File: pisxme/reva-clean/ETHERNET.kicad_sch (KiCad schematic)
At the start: 0 parts

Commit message: add native Phase 3 contract connectivity
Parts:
- added X: ETHERNET_Contract
- added XET: ETHERNET_Contract, symbol PiSXMeRevAClean:ETHERNET_Contract
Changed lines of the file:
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@@
 (kicad_sch (version 20230409) (generator "eeschema")
   (paper "A4")
+    (symbol "PiSXMeRevAClean:ETHERNET_Contract"
+      (pin_names (offset 1.0))
+      (exclude_from_sim no)
+      (in_bom yes)
+      (on_board yes)
+      (property "Reference" "X"
+        (at 0 -7.039999999999999 0)
+        (effects (font (size 1.27 1.27))))
+      (property "Value" "ETHERNET_Contract"
+        (at 0 7.039999999999999 0)
+        (effects (font (size 1.27 1.27))))
+      (property "Footprint" ""
+        (at 0 0 0)
+        (effects (font (size 1.27 1.27)) (hide yes)))
+      (property "Datasheet" "~"
+        (at 0 0 0)
+        (effects (font (size 1.27 1.27)) (hide yes)))
+      (symbol "ETHERNET_Contract_1_1"
+        (rectangle (start -1.27 -5.77) (end 1.27 5.77)
+          (stroke (width 0.254) (type default)) (fill (type background)))
+        (pin passive line
+          (at -5.08 0 0)
+          (length 3.81)
+          (name "CM5_GBE" (effects (font (size 1.27 1.27))))
+          (number "1" (effects (font (size 1.27 1.27)))))
+        (pin passive line
+          (at -5.08 3 0)
+          (length 3.81)
+          (name "GBE_LED" (effects (font (size 1.27 1.27))))
+          (number "2" (effects (font (size 1.27 1.27)))))
+        (pin passive line
+          (at -5.08 6 0)
+          (length 3.81)
+          (name "GBE_SHIELD" (effects (font (size 1.27 1.27))))
+          (number "3" (effects (font (size 1.27 1.27)))))
+        (pin passive line
+          (at -5.08 9 0)
+          (length 3.81)
+          (name "ETH_POWER" (effects (font (size 1.27 1.27))))
+          (number "4" (effects (font (size 1.27 1.27)))))
+      )
+    )
   (hierarchical_label "CM5_GBE"
     (shape bidirectional)
@@
     (effects (font (size 1.27 1.27)) (justify left))
 )
-  (sheet_instances (path "/6" (page "6")))
+  (wire
+    (pts (xy 5 10) (xy 19.92 10))
+    (stroke (width 0) (type default))
 )
+  (wire
+    (pts (xy 5 13) (xy 19.92 13))
+    (stroke (width 0) (type default))
+)
+  (wire
+    (pts (xy 5 16) (xy 19.92 16))
+    (stroke (width 0) (type default))
+)
+  (wire
+    (pts (xy 5 19) (xy 19.92 19))
+    (stroke (width 0) (type default))
+)
+  (symbol
+    (lib_id "PiSXMeRevAClean:ETHERNET_Contract")
+    (at 25 10 0)
+    (unit 1)
+    (exclude_from_sim no)
+    (in_bom no)
+    (on_board no)
+    (dnp no)
+    (property "Reference" "XET"
+      (at 25 5 0)
+      (effects (font (size 1.27 1.27))))
+    (property "Value" "ETHERNET_Contract"
+      (at 25 18 0)
+      (effects (font (size 1.27 1.27))))
+    (property "Footprint" ""
+      (at 25 10 0)
+      (effects (font (size 1.27 1.27)) (hide yes)))
+    (property "Datasheet" "~"
+      (at 25 10 0)
+      (effects (font (size 1.27 1.27)) (hide yes)))
+    (pin "1")
+    (pin "2")
+    (pin "3")
+    (pin "4")
+    (instances (project "PiSXMe_RevA_Clean"
+      (path "/30000000-0000-0000-0000-000000000000/10000000-0000-0000-0000-000000000006" (reference "XET" ) (unit 1))))
+  )
+  (sheet_instances (path "/30000000-0000-0000-0000-000000000000/10000000-0000-0000-0000-000000000006" (page "6")))
+)

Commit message: close native Phase 3 hierarchy association
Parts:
- removed X: ETHERNET_Contract
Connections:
- net CM5_GBE: now also XET.1 (CM5_GBE)
- net ETH_POWER: now also XET.4 (ETH_POWER)
- net GBE_LED: now also XET.2 (GBE_LED)
- net GBE_SHIELD: now also XET.3 (GBE_SHIELD)
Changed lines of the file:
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@@
 (kicad_sch (version 20230409) (generator "eeschema")
   (paper "A4")
-    (symbol "PiSXMeRevAClean:ETHERNET_Contract"
-      (pin_names (offset 1.0))
-      (exclude_from_sim no)
-      (in_bom yes)
-      (on_board yes)
-      (property "Reference" "X"
-        (at 0 -7.039999999999999 0)
-        (effects (font (size 1.27 1.27))))
-      (property "Value" "ETHERNET_Contract"
-        (at 0 7.039999999999999 0)
-        (effects (font (size 1.27 1.27))))
-      (property "Footprint" ""
-        (at 0 0 0)
-        (effects (font (size 1.27 1.27)) (hide yes)))
-      (property "Datasheet" "~"
-        (at 0 0 0)
-        (effects (font (size 1.27 1.27)) (hide yes)))
-      (symbol "ETHERNET_Contract_1_1"
-        (rectangle (start -1.27 -5.77) (end 1.27 5.77)
-          (stroke (width 0.254) (type default)) (fill (type background)))
-        (pin passive line
-          (at -5.08 0 0)
-          (length 3.81)
-          (name "CM5_GBE" (effects (font (size 1.27 1.27))))
-          (number "1" (effects (font (size 1.27 1.27)))))
-        (pin passive line
-          (at -5.08 3 0)
-          (length 3.81)
-          (name "GBE_LED" (effects (font (size 1.27 1.27))))
-          (number "2" (effects (font (size 1.27 1.27)))))
-        (pin passive line
-          (at -5.08 6 0)
-          (length 3.81)
-          (name "GBE_SHIELD" (effects (font (size 1.27 1.27))))
-          (number "3" (effects (font (size 1.27 1.27)))))
-        (pin passive line
-          (at -5.08 9 0)
-          (length 3.81)
-          (name "ETH_POWER" (effects (font (size 1.27 1.27))))
-          (number "4" (effects (font (size 1.27 1.27)))))
-      )
-    )
   (hierarchical_label "CM5_GBE"
     (shape bidirectional)
-    (at 5 10 0)
-    (effects (font (size 1.27 1.27)) (justify left))
+    (at 5 10 180)
+    (effects (font (size 1.27 1.27)) (justify right))
 )
   (hierarchical_label "GBE_LED"
     (shape bidirectional)
-    (at 5 13 0)
-    (effects (font (size 1.27 1.27)) (justify left))
+    (at 5 13 180)
+    (effects (font (size 1.27 1.27)) (justify right))
 )
   (hierarchical_label "GBE_SHIELD"
     (shape bidirectional)
-    (at 5 16 0)
-    (effects (font (size 1.27 1.27)) (justify left))
+    (at 5 16 180)
+    (effects (font (size 1.27 1.27)) (justify right))
 )
   (hierarchical_label "ETH_POWER"
     (shape bidirectional)
-    (at 5 19 0)
-    (effects (font (size 1.27 1.27)) (justify left))
+    (at 5 19 180)
+    (effects (font (size 1.27 1.27)) (justify right))
 )
   (wire

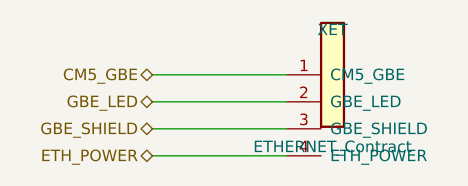
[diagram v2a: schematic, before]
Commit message: stabilize Phase 3 hierarchy netlist references
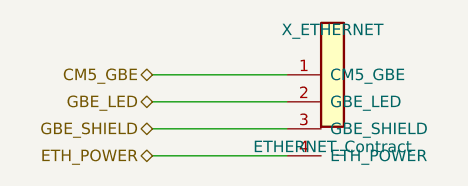
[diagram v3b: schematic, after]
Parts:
- renumbered XET to X_ETHERNET
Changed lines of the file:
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@@
     (on_board no)
     (dnp no)
-    (property "Reference" "XET"
+    (property "Reference" "X_ETHERNET"
       (at 25 5 0)
       (effects (font (size 1.27 1.27))))
@@
     (pin "4")
     (instances (project "PiSXMe_RevA_Clean"
-      (path "/30000000-0000-0000-0000-000000000000/10000000-0000-0000-0000-000000000006" (reference "XET" ) (unit 1))))
+      (path "/30000000-0000-0000-0000-000000000000/10000000-0000-0000-0000-000000000006" (reference "X_ETHERNET" ) (unit 1))))
   )
   (sheet_instances (path "/30000000-0000-0000-0000-000000000000/10000000-0000-0000-0000-000000000006" (page "6")))

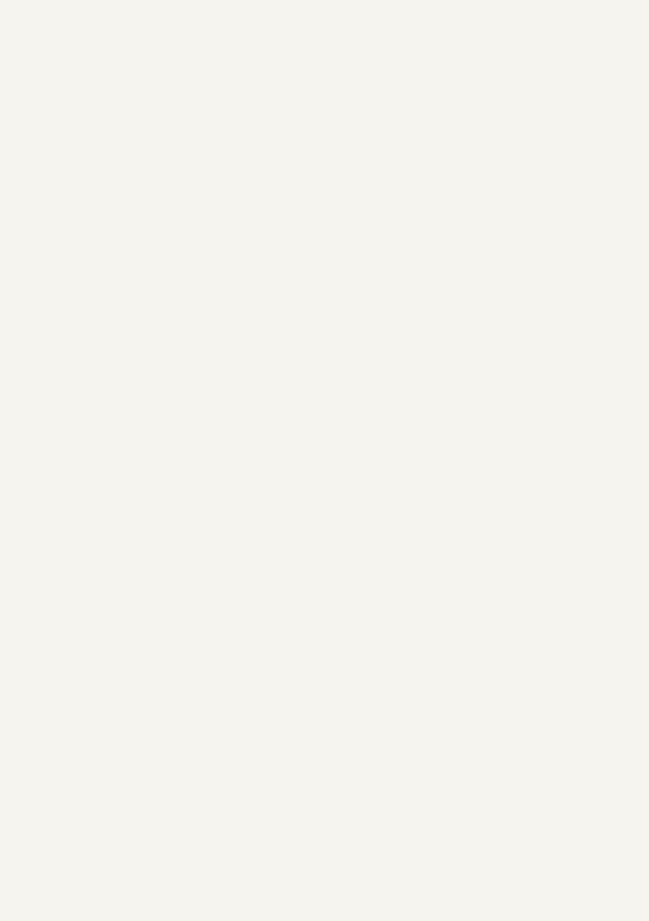
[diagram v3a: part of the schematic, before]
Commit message: close Phase 6 Ethernet island
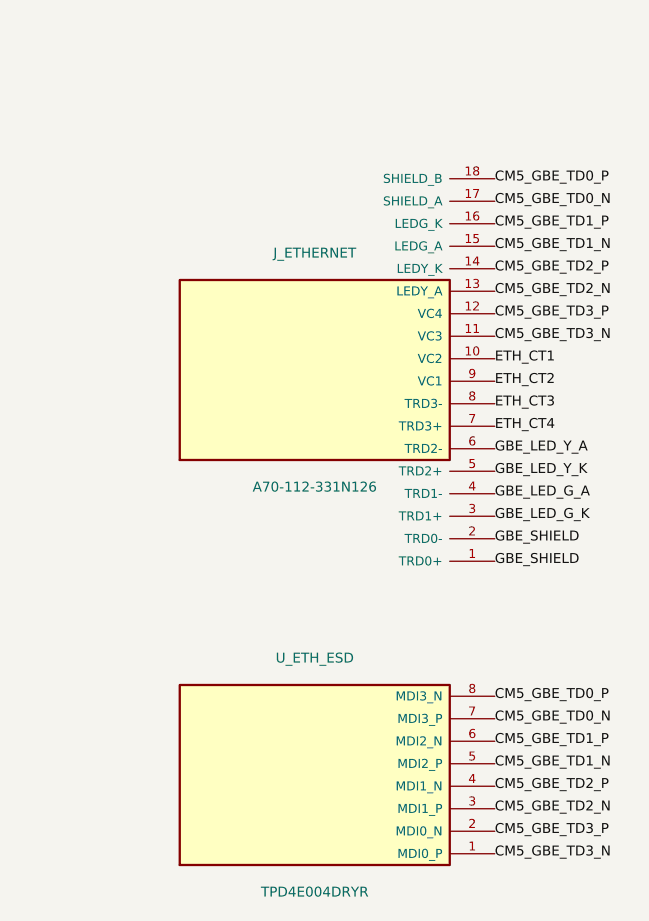
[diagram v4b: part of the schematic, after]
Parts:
- added J_ETHERNET: A70-112-331N126, PiSXMeRevAClean:EDAC_A70_112_331N126, symbol PiSXMeRevAClean:EDAC_A70_112_331N126_Ethernet
- added U_ETH_ESD: TPD4E004DRYR, Package_DFN_QFN:WSON-6-1EP_1.5x1.5mm_P0.5mm_EP0.95x0.95mm, symbol PiSXMeRevAClean:TPD4E004DRYR
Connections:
- net GBE_SHIELD: now also J_ETHERNET.1 (TRD0+), J_ETHERNET.2 (TRD0-)
- new net CM5_GBE_TD0_N: J_ETHERNET.17 (SHIELD_A), U_ETH_ESD.7 (MDI3_P)
- new net CM5_GBE_TD0_P: J_ETHERNET.18 (SHIELD_B), U_ETH_ESD.8 (MDI3_N)
- new net CM5_GBE_TD1_N: J_ETHERNET.15 (LEDG_A), U_ETH_ESD.5 (MDI2_P)
- new net CM5_GBE_TD1_P: J_ETHERNET.16 (LEDG_K), U_ETH_ESD.6 (MDI2_N)
- new net CM5_GBE_TD2_N: J_ETHERNET.13 (LEDY_A), U_ETH_ESD.3 (MDI1_P)
- new net CM5_GBE_TD2_P: J_ETHERNET.14 (LEDY_K), U_ETH_ESD.4 (MDI1_N)
- new net CM5_GBE_TD3_N: J_ETHERNET.11 (VC3), U_ETH_ESD.1 (MDI0_P)
- new net CM5_GBE_TD3_P: J_ETHERNET.12 (VC4), U_ETH_ESD.2 (MDI0_N)
- new net ETH_CT1: J_ETHERNET.10 (VC2)
- new net ETH_CT2: J_ETHERNET.9 (VC1)
- new net ETH_CT3: J_ETHERNET.8 (TRD3-)
- new net ETH_CT4: J_ETHERNET.7 (TRD3+)
- new net GBE_LED_G_A: J_ETHERNET.4 (TRD1-)
- new net GBE_LED_G_K: J_ETHERNET.3 (TRD1+)
- new net GBE_LED_Y_A: J_ETHERNET.6 (TRD2-)
- new net GBE_LED_Y_K: J_ETHERNET.5 (TRD2+)
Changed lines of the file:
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@@
       (path "/30000000-0000-0000-0000-000000000000/10000000-0000-0000-0000-000000000006" (reference "X_ETHERNET" ) (unit 1))))
   )
+(label "CM5_GBE_TD0_P" (at 70 78.75 0) (effects (font (size 1.1 1.1)) (justify left)))
+(label "CM5_GBE_TD0_N" (at 70 81.25 0) (effects (font (size 1.1 1.1)) (justify left)))
+(label "CM5_GBE_TD1_P" (at 70 83.75 0) (effects (font (size 1.1 1.1)) (justify left)))
+(label "CM5_GBE_TD1_N" (at 70 86.25 0) (effects (font (size 1.1 1.1)) (justify left)))
+(label "CM5_GBE_TD2_P" (at 70 88.75 0) (effects (font (size 1.1 1.1)) (justify left)))
+(label "CM5_GBE_TD2_N" (at 70 91.25 0) (effects (font (size 1.1 1.1)) (justify left)))
+(label "CM5_GBE_TD3_P" (at 70 93.75 0) (effects (font (size 1.1 1.1)) (justify left)))
+(label "CM5_GBE_TD3_N" (at 70 96.25 0) (effects (font (size 1.1 1.1)) (justify left)))
+(label "ETH_CT1" (at 70 98.75 0) (effects (font (size 1.1 1.1)) (justify left)))
+(label "ETH_CT2" (at 70 101.25 0) (effects (font (size 1.1 1.1)) (justify left)))
+(label "ETH_CT3" (at 70 103.75 0) (effects (font (size 1.1 1.1)) (justify left)))
+(label "ETH_CT4" (at 70 106.25 0) (effects (font (size 1.1 1.1)) (justify left)))
+(label "GBE_LED_Y_A" (at 70 108.75 0) (effects (font (size 1.1 1.1)) (justify left)))
+(label "GBE_LED_Y_K" (at 70 111.25 0) (effects (font (size 1.1 1.1)) (justify left)))
+(label "GBE_LED_G_A" (at 70 113.75 0) (effects (font (size 1.1 1.1)) (justify left)))
+(label "GBE_LED_G_K" (at 70 116.25 0) (effects (font (size 1.1 1.1)) (justify left)))
+(label "GBE_SHIELD" (at 70 118.75 0) (effects (font (size 1.1 1.1)) (justify left)))
+(label "GBE_SHIELD" (at 70 121.25 0) (effects (font (size 1.1 1.1)) (justify left)))
+(symbol (lib_id "PiSXMeRevAClean:EDAC_A70_112_331N126_Ethernet") (at 50 100 0) (unit 1) (exclude_from_sim no) (in_bom yes) (on_board yes) (dnp no) (property "Reference" "J_ETHERNET" (at 50 87 0) (effects (font (size 1.1 1.1)))) (property "Value" "A70-112-331N126" (at 50 113 0) (effects (font (size 1.1 1.1)))) (property "MPN" "A70-112-331N126" (at 50 100 0) (effects (font (size 1 1)) (hide yes))) (property "Footprint" "PiSXMeRevAClean:EDAC_A70_112_331N126" (at 50 100 0) (effects (font (size 1 1)) (hide yes))) (pin "1")
+(pin "2")
+(pin "3")
+(pin "4")
+(pin "5")
+(pin "6")
+(pin "7")
+(pin "8")
+(pin "9")
+(pin "10")
+(pin "11")
+(pin "12")
+(pin "13")
+(pin "14")
+(pin "15")
+(pin "16")
+(pin "17")
+(pin "18") (instances (project "PiSXMe_RevA_Clean" (path "/30000000-0000-0000-0000-000000000000" (reference "J_ETHERNET") (unit 1)))) )(label "CM5_GBE_TD0_P" (at 70 136.25 0) (effects (font (size 1.1 1.1)) (justify left)))
+(label "CM5_GBE_TD0_N" (at 70 138.75 0) (effects (font (size 1.1 1.1)) (justify left)))
+(label "CM5_GBE_TD1_P" (at 70 141.25 0) (effects (font (size 1.1 1.1)) (justify left)))
+(label "CM5_GBE_TD1_N" (at 70 143.75 0) (effects (font (size 1.1 1.1)) (justify left)))
+(label "CM5_GBE_TD2_P" (at 70 146.25 0) (effects (font (size 1.1 1.1)) (justify left)))
+(label "CM5_GBE_TD2_N" (at 70 148.75 0) (effects (font (size 1.1 1.1)) (justify left)))
+(label "CM5_GBE_TD3_P" (at 70 151.25 0) (effects (font (size 1.1 1.1)) (justify left)))
+(label "CM5_GBE_TD3_N" (at 70 153.75 0) (effects (font (size 1.1 1.1)) (justify left)))
+(symbol (lib_id "PiSXMeRevAClean:TPD4E004DRYR") (at 50 145 0) (unit 1) (exclude_from_sim no) (in_bom yes) (on_board yes) (dnp no) (property "Reference" "U_ETH_ESD" (at 50 132 0) (effects (font (size 1.1 1.1)))) (property "Value" "TPD4E004DRYR" (at 50 158 0) (effects (font (size 1.1 1.1)))) (property "MPN" "TPD4E004DRYR" (at 50 145 0) (effects (font (size 1 1)) (hide yes))) (property "Footprint" "Package_DFN_QFN:WSON-6-1EP_1.5x1.5mm_P0.5mm_EP0.95x0.95mm" (at 50 145 0) (effects (font (size 1 1)) (hide yes))) (pin "1")
+(pin "2")
+(pin "3")
+(pin "4")
+(pin "5")
+(pin "6")
+(pin "7")
+(pin "8") (instances (project "PiSXMe_RevA_Clean" (path "/30000000-0000-0000-0000-000000000000" (reference "U_ETH_ESD") (unit 1)))) )
   (sheet_instances (path "/30000000-0000-0000-0000-000000000000/10000000-0000-0000-0000-000000000006" (page "6")))
 )

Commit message: start phase 14 footprint authority
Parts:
- U_ETH_ESD: footprint Package_DFN_QFN:WSON-6-1EP_1.5x1.5mm_P0.5mm_EP0.95x0.95mm -> PiSXMeRevAClean:TPD4E004DRYR_WSON6
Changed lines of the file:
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@@
 (label "CM5_GBE_TD3_P" (at 70 151.25 0) (effects (font (size 1.1 1.1)) (justify left)))
 (label "CM5_GBE_TD3_N" (at 70 153.75 0) (effects (font (size 1.1 1.1)) (justify left)))
-(symbol (lib_id "PiSXMeRevAClean:TPD4E004DRYR") (at 50 145 0) (unit 1) (exclude_from_sim no) (in_bom yes) (on_board yes) (dnp no) (property "Reference" "U_ETH_ESD" (at 50 132 0) (effects (font (size 1.1 1.1)))) (property "Value" "TPD4E004DRYR" (at 50 158 0) (effects (font (size 1.1 1.1)))) (property "MPN" "TPD4E004DRYR" (at 50 145 0) (effects (font (size 1 1)) (hide yes))) (property "Footprint" "Package_DFN_QFN:WSON-6-1EP_1.5x1.5mm_P0.5mm_EP0.95x0.95mm" (at 50 145 0) (effects (font (size 1 1)) (hide yes))) (pin "1")
+(symbol (lib_id "PiSXMeRevAClean:TPD4E004DRYR") (at 50 145 0) (unit 1) (exclude_from_sim no) (in_bom yes) (on_board yes) (dnp no) (property "Reference" "U_ETH_ESD" (at 50 132 0) (effects (font (size 1.1 1.1)))) (property "Value" "TPD4E004DRYR" (at 50 158 0) (effects (font (size 1.1 1.1)))) (property "MPN" "TPD4E004DRYR" (at 50 145 0) (effects (font (size 1 1)) (hide yes))) (property "Footprint" "PiSXMeRevAClean:TPD4E004DRYR_WSON6" (at 50 145 0) (effects (font (size 1 1)) (hide yes))) (pin "1")
 (pin "2")
 (pin "3")
